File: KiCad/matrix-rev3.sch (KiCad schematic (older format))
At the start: 147 parts

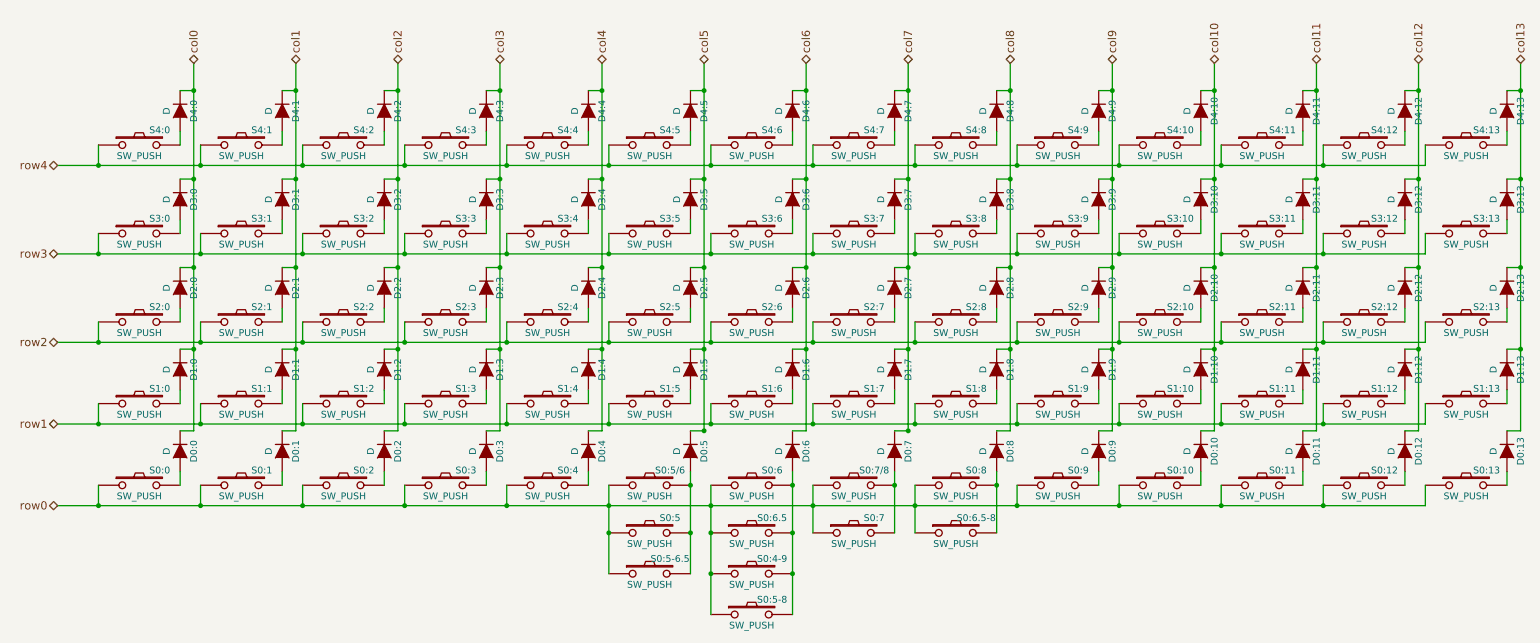
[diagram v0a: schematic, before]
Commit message: adding prototype for revision 3: with more support for other layouts
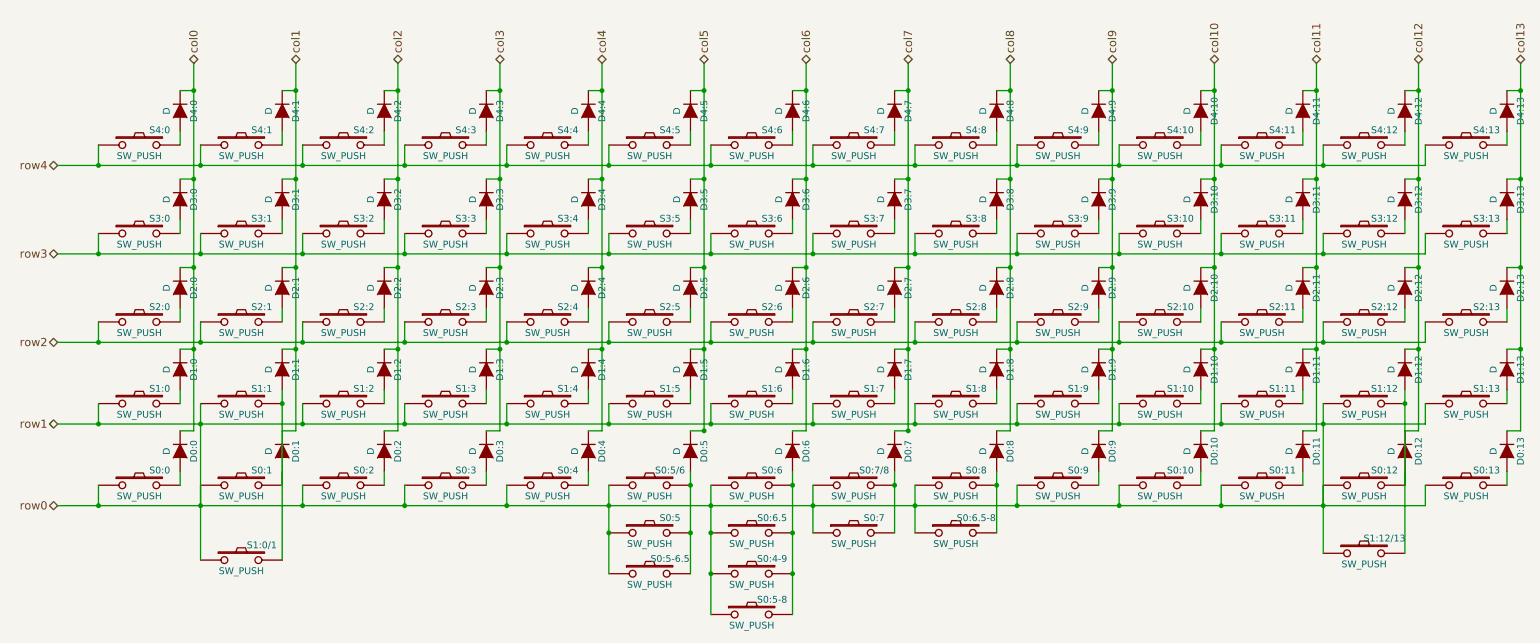
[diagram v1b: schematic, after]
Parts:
- added S1:0/1, S1:12/13: SW_PUSH, symbol SW_PUSH
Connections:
- net row1 is gone; now on net row0: S1:0.1, S1:1.1, S1:10.1, S1:11.1, S1:12.1, S1:13.1, S1:2.1, S1:3.1, S1:4.1, S1:5.1, S1:6.1, S1:7.1, S1:8.1, S1:9.1
- net row0: now also S1:0/1.1, S1:12/13.1
- net at D1:12.2 (A), S1:12.2: now also D0:12.2 (A), S0:12.2, S1:12/13.2
- net at D0:1.2 (A), S0:1.2: now also D1:1.2 (A), S1:1.2, S1:0/1.2
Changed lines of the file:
@@
 LIBS:components
 LIBS:keyboard-cache
+LIBS:keyboard-rev3-cache
 EELAYER 25 0
 EELAYER END
@@
 Connection ~ 3200 5850
 Wire Wire Line
-	3200 5850 3200 5700
+	3200 5700 3200 6850
 Connection ~ 3950 5850
 Wire Wire Line
@@
 	10700 5850 10700 5700
 Wire Wire Line
-	11450 5850 11450 5700
+	11450 5700 11450 6800
 Wire Wire Line
 	12200 5850 12200 5700
@@
 	11300 6300 11300 6200
 Wire Wire Line
-	12050 5700 12050 5600
+	12050 5600 12050 6800
 Wire Wire Line
 	11300 5700 11300 5600
@@
 	3050 5700 3050 5600
 Wire Wire Line
-	3800 5700 3800 5600
+	3800 5600 3800 6850
 Wire Wire Line
 	4550 5700 4550 5600
@@
 Connection ~ 7550 6950
 Connection ~ 9050 6300
+$Comp
+L SW_PUSH S1:12/13
+U 1 1 58E17B47
+P 11750 6800
+F 0 "S1:12/13" H 11900 6910 50  0000 C CNN
+F 1 "SW_PUSH" H 11750 6720 50  0000 C CNN
+F 2 "" H 11750 6800 50  0000 C CNN
+F 3 "" H 11750 6800 50  0000 C CNN
+	1    11750 6800
+	1    0    0    -1
+$EndComp
+Connection ~ 12050 5700
+$Comp
+L SW_PUSH S1:0/1
+U 1 1 58E1C383
+P 3500 6850
+F 0 "S1:0/1" H 3650 6960 50  0000 C CNN
+F 1 "SW_PUSH" H 3500 6770 50  0000 C CNN
+F 2 "" H 3500 6850 50  0000 C CNN
+F 3 "" H 3500 6850 50  0000 C CNN
+	1    3500 6850
+	1    0    0    -1
+$EndComp
+Connection ~ 3800 5700
 $EndSCHEMATC
